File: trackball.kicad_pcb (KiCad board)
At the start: 6 copper layers, 65 x 85 mm, 241 parts, among them J2 ZX-PM2.0-2-4PY, Q1 XR2302, Q2 XR2302, SW1 HX TC-5608-Y, SW2 HX TC-5608-Y, SW3 HX TC-5608-Y, SW4 HX TC-5608-Y, SW5 HX TC-5608-Y, SW6 HX TC-5608-Y, SW7 HX TC-5608-Y, SW8 HX TC-5608-Y, SW9 TS-1010-C-A, U1 USB-TYPE-C-017, U10 WS2812B, U11 WS2812B, U12 WS2812B, U13 WS2812B, U14 WS2812B, U15 WS2812B, U16 WS2812B, U17 WS2812B, U18 WS2812B, U19 WS2812B, U2 SY80004DQD, U20 WS2812B, U21 WS2812B, U3 SY80004DQD, U4 PMW3610, U5 PMW3610, U6 WS2812B, U7 WS2812B, U8 WS2812B, U9 WS2812B, X1 XL7EL89CKI-111YLC-32M

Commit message: bugfix: 3d models
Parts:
- moved R5 0.13 mm to (36.7, 60.6)
- moved R24 0.11 mm to (37.7, 60.6)
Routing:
- net 1V8: track 307.1 -> 308.7 mm

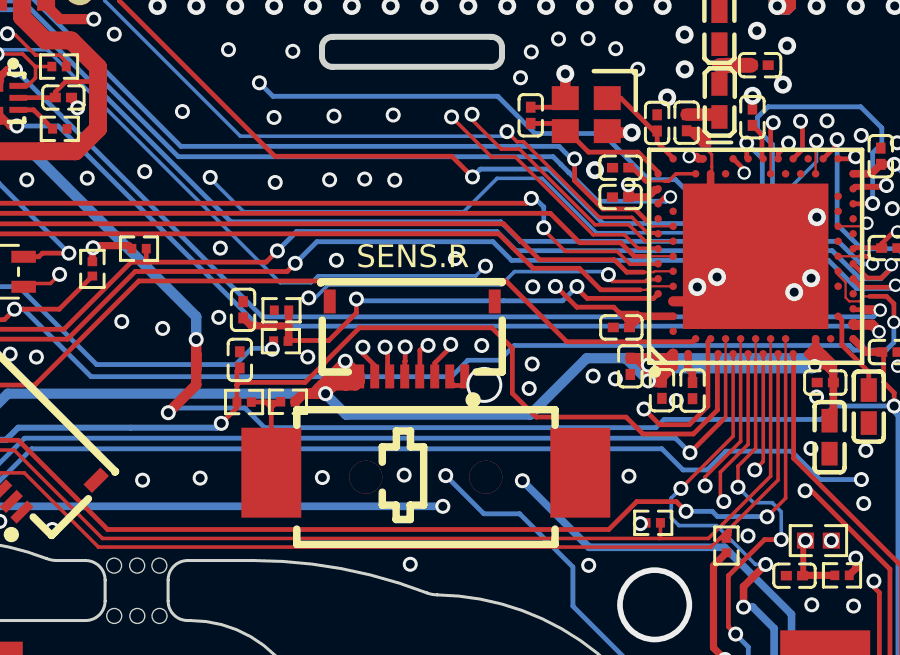
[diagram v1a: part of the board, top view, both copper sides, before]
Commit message: feat: encoders upgrade; PAW3395 bb; PAW3805 bb
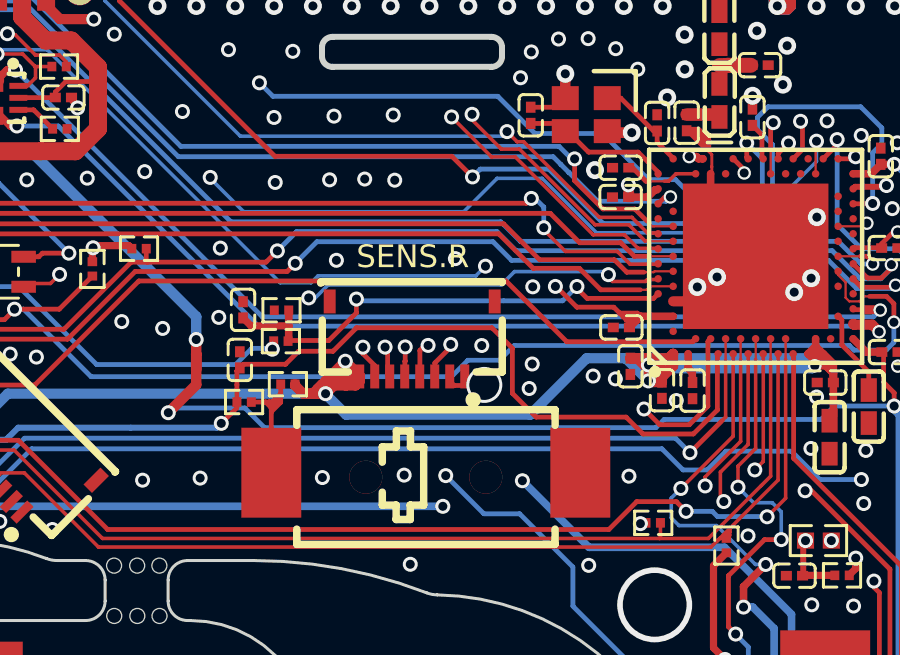
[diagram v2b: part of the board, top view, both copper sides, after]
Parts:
- moved R37 0.59 mm to (76.2, 55.6)
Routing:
- net Net-(R19-Pad1): track 3.94 -> 5.63 mm
- net GND: vias 348 -> 347
